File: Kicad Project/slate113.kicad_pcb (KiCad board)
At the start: 8 copper layers, 212.7 x 126.2 mm, 633 parts, among them CN1 DF40C-50DP-0.4V, CN10 DF40C-40DP-0.4V, CN11 DF40C-30DP-0.4V, CN12 DF40C-50DS-0.4V, CN13 DF40C-50DS-0.4V, CN14 DF40C-30DP-0.4V, CN15 DF40C-24DS-0.4V, CN16 DF40C-24DS-0.4V, CN17 530480310, CN18 DF40C-10DP-0.4V, CN19 DF40C-24DP-0.4V, CN2 DF40C-50DP-0.4V, CN20 DF40C-24DP-0.4V, CN21 DF40C-40DS-0.4V, CN22 DF40C-40DS-0.4V, CN3 DF40C-30DS-0.4V, CN4 DF40C-40DS-0.4V, CN5 DF40C-40DP-0.4V, CN6 DF40C-40DS-0.4V, CN7 DF40C-30DS-0.4V, CN8 DF40C-40DP-0.4V, CN9 DF40C-40DP-0.4V, J1 RFPC-SMA27-F, J10 Conn_Coaxial, J11 RFPC-SMA27-F, J12 Conn_Coaxial, J13 U.FL, J14 U.FL, J15 U.FL, J16 U.FL, J17 U.FL, J18 U.FL, J19 U.FL, J2 TYPE-C16PIN, J20 U.FL, J22 RFPC-SMA27-F, J23 RFPC-SMA27-F, J24 Conn_Coaxial, J25 RFPC-SMA27-F, J26 Conn_Coaxial, J3 Conn_Coaxial, J4 DF40C-100DP-0.4V51*2, J6 395-016-520-202, J7 Conn_Coaxial, J8 RFPC-SMA27-F, J9 Bus_M.2_Socket_B, Q1 MMBT3904-TP, Q4 MMBT3904-C20526, Q5 CSD17575Q3, Q6 CSD17575Q3, Q7 CSD17575Q3, Q8 CSD17575Q3, SW1 SW_Push, SW2 SW_Push, SW3 SW_Push, SW4 SW_Push, U1 FUSB302BMPX, U10 TS3A24159DGSR, U11 SiP32508DT, U12 PI3USB302-AZBEX, U13 W25Q32JVSSIQ, U14 SiP32508DT, U15 TS5A23157DGSR, U17 SiP32508DT, U18 GL3523-OTY3C, U19 TXM27.12M0004322DBBDO00T, U2 CH224K, U20 CC1101RGPR, U21 0896BM15A0001001E, U22 LC29HBA, U23 EM4095HMSO16B+, U24 PE4259-63, U25 PE4259-63, U26 PE4259-63, U27 PE4259-63, U28 0433BM15A0001001E, U29 PN7160A1HN/C100E, U3 BQ25792RQMR, U30 PE4259-63, U31 B2B-PH-K-S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

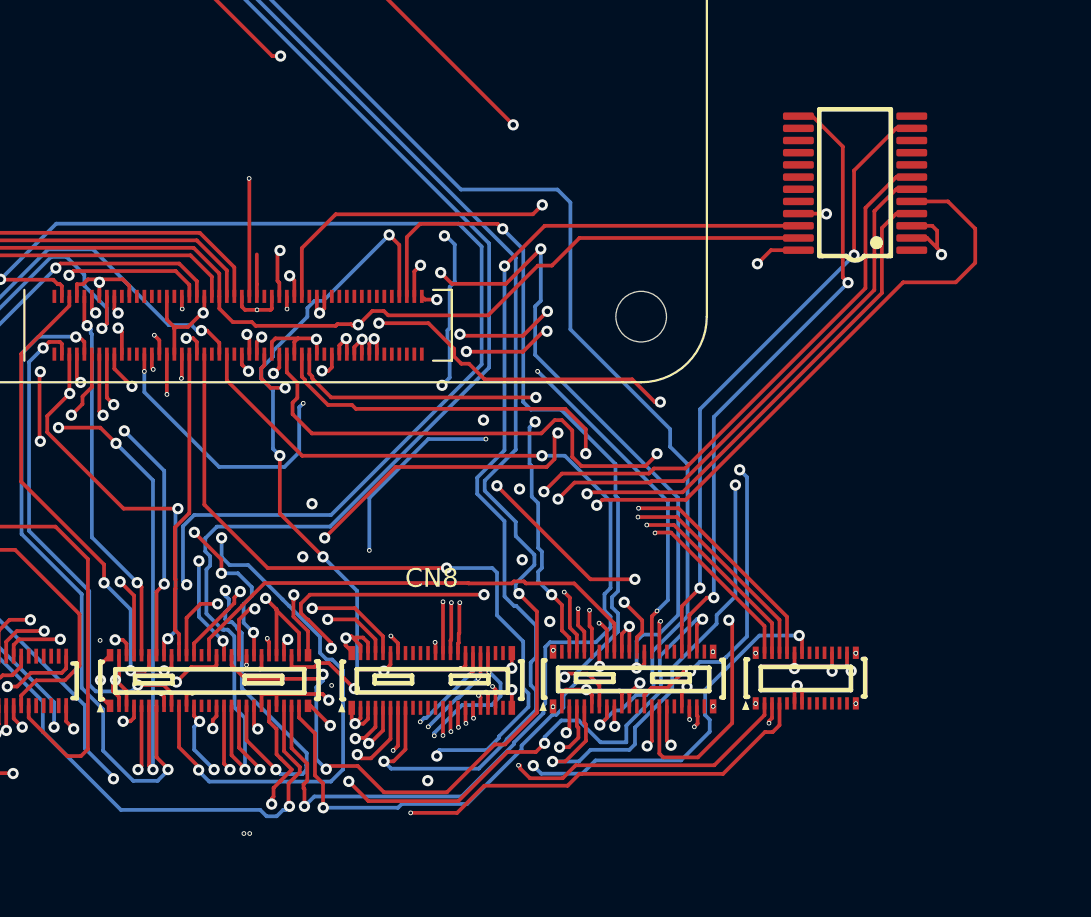
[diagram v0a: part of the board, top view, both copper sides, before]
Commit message: worked on the carrier board more and finish up the radio b2b connector (excluding LED stuff)
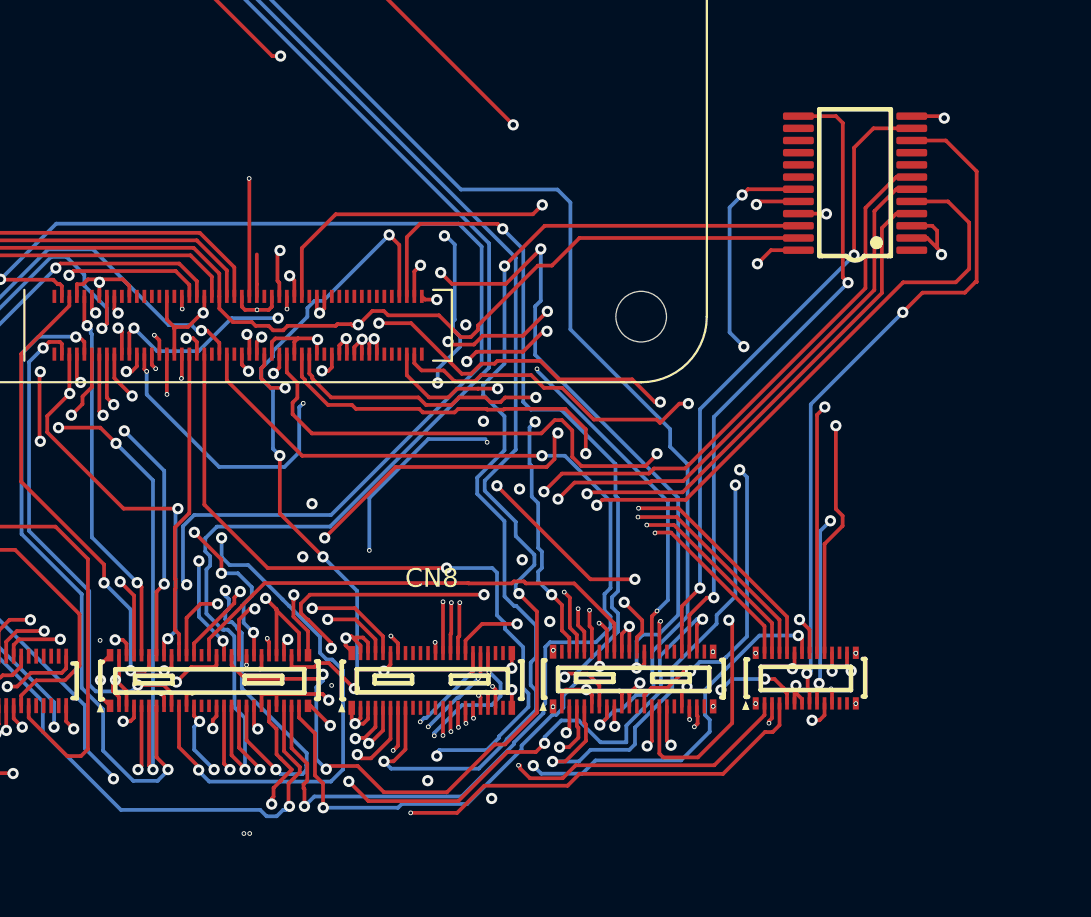
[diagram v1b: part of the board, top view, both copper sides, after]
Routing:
- net CM5_UART_TX: track 25.7 -> 82.8 mm, vias 2 -> 6
- net RADIO_EN: track 31.0 -> 68.7 mm, vias 2 -> 4
- net ESP_RST: track 37.1 -> 74.4 mm, vias 2 -> 5
- net CM5_UART_RX: track 26.1 -> 61.6 mm, vias 2 -> 4
- net RP_ACC_SCK: track 146.9 -> 180.1 mm, vias 9 -> 12
- net RF_V2: track 91.6 -> 122.7 mm, vias 5 -> 8
- net RF_V1: track 78.4 -> 107.1 mm, vias 4 -> 6
- net GND: track 467.0 -> 470.1 mm, vias 307 -> 309
- net 3V3: track 332.4 -> 334.4 mm, vias 41 -> 42
- net TYPEC_AUXP: track 87.5 -> 88.8 mm
- net I2C0_SDA: track 219.5 -> 220.8 mm
- net SD_CLK: track 99.3 -> 100.3 mm
- net PCIE0_WAKE: track 83.9 -> 84.8 mm
- net I2C0_SCL: track 212.2 -> 213.2 mm
- net CM5_ACC_RESET_N: track 109.8 -> 110.7 mm
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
